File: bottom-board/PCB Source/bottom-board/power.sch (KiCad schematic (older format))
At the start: 22 parts, among them P3 BARREL_JACK, U1 TS2596, U2 TL750M10CKVURG3, U9 LD1117S50TR_SOT223

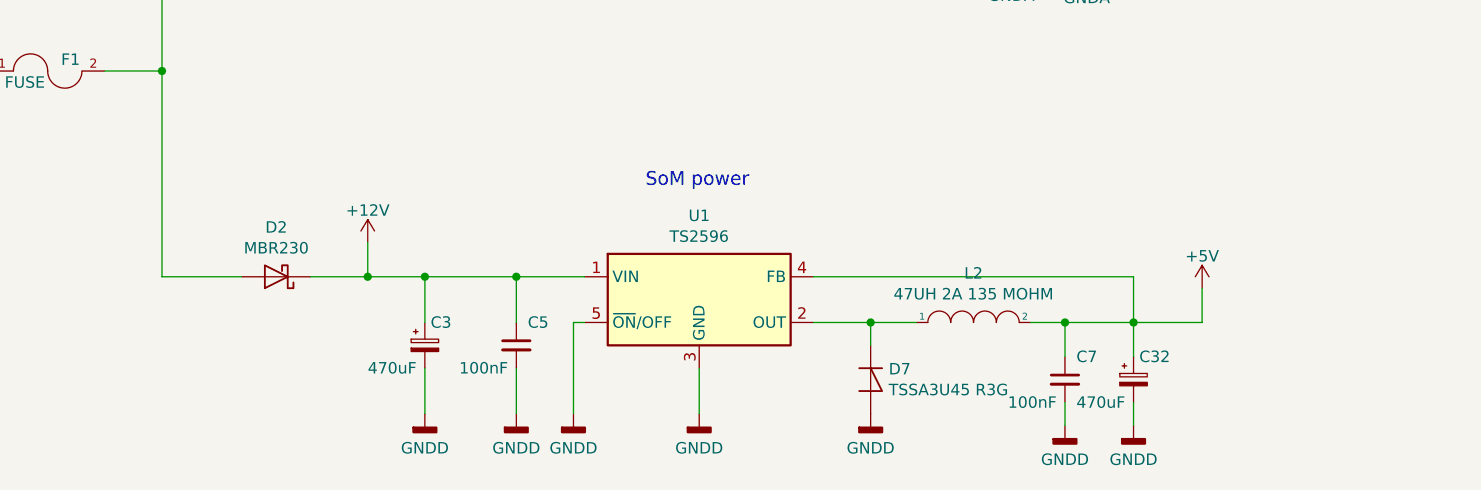
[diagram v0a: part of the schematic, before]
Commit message: increase som filter caps
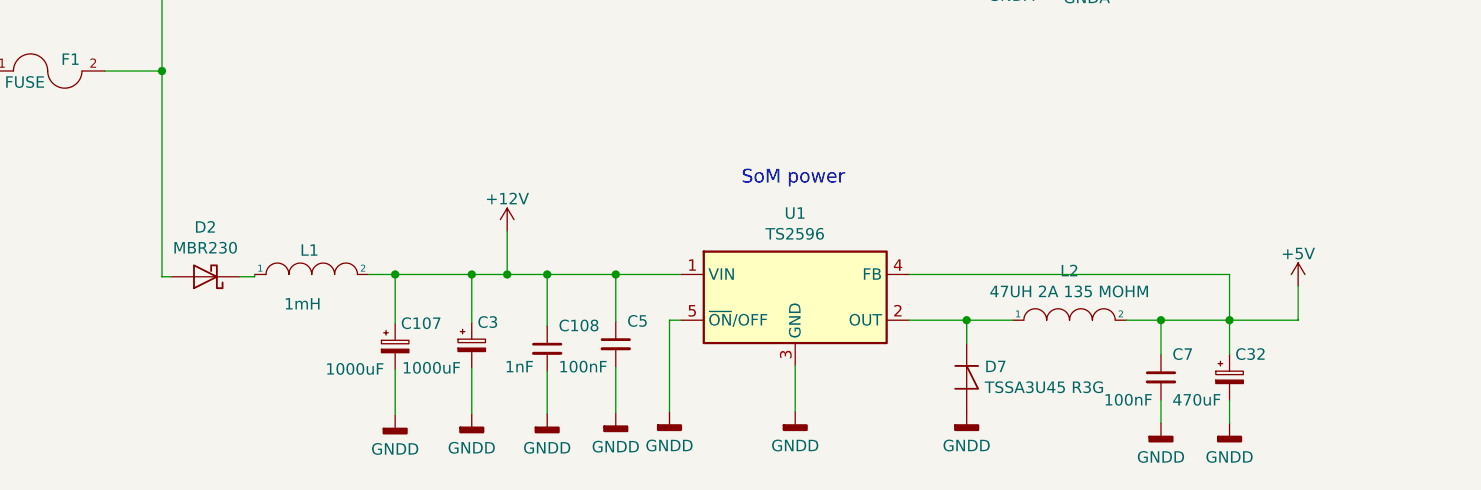
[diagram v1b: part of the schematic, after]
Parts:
- added C107: 1000uF, Uno:CAPAE1300X1400N, symbol bottom-board-rescue:CP_Small
- added C108: 1nF, Capacitor_SMD:C_0603_1608Metric, symbol bottom-board-rescue:C_Small
- added L1: 1mH, Inductor_SMD:L_Bourns_SRR1260, symbol bottom-board-rescue:INDUCTOR-pspice
- C3: value 470uF -> 1000uF; footprint Capacitor_SMD:CP_Elec_8x10.5 -> Uno:CAPAE1300X1400N; MPN UWT1C471MNL1GS -> VE-102M1CTR-1313S
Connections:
- net +12V: now also C107.1, C108.1, L1.2; no longer D2.1 (K)
- net GNDD: now also C107.2, C108.2
- new net: D2.1 (K), L1.1
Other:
- moved on the sheet: C3, C32, C5, C7, D2, D7, L2, U1

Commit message: update fabrication data
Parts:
- U9: MPN (none) -> LD1117S50TR
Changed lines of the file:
@@
 F 2 "Package_TO_SOT_SMD:SOT-223-3_TabPin2" H 6430 3825 50  0001 C CNN
 F 3 "http://www.st.com/st-web-ui/static/active/en/resource/technical/document/datasheet/CD00000544.pdf" H 6530 3375 50  0001 C CNN
+F 4 "LD1117S50TR" H 6430 3625 50  0001 C CNN "MPN"
 	1    6430 3625
 	1    0    0    -1

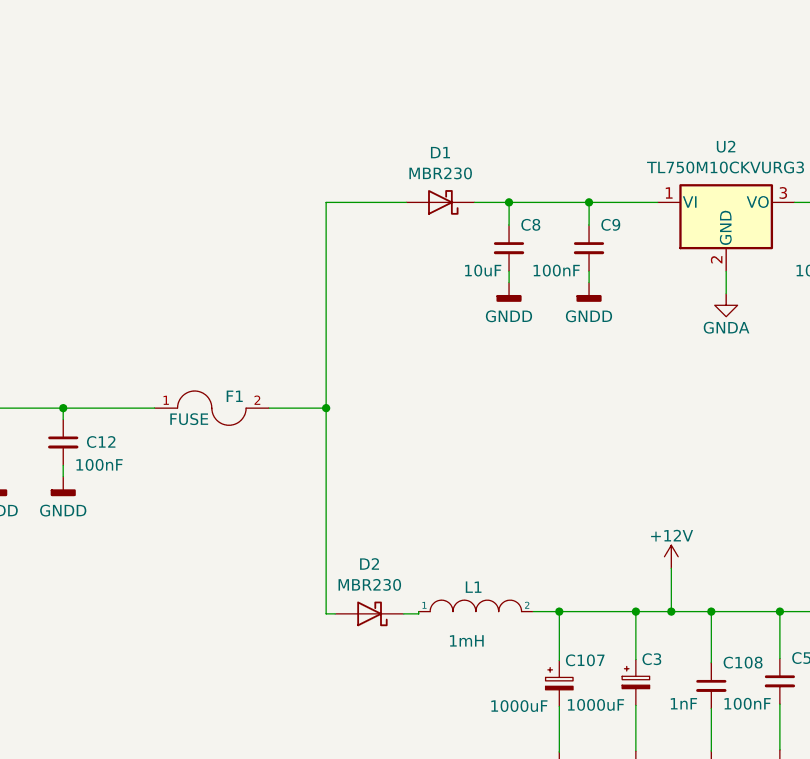
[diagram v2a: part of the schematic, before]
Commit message: change input bias 5->6V, reduce harmonics
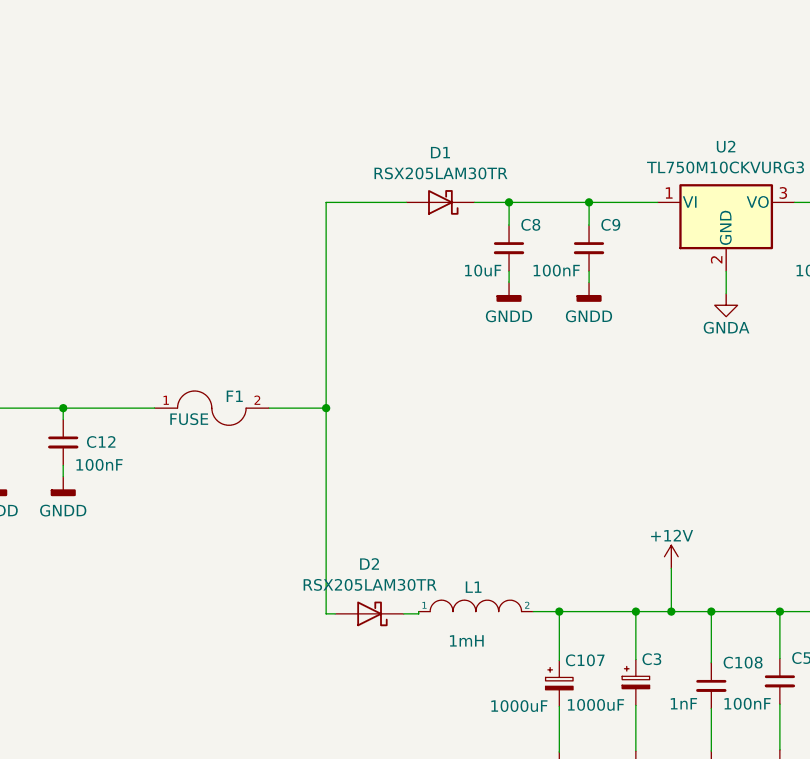
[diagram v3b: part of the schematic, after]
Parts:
- C1: MPN UWX1C101MCL1GB -> 107SML016M
- C107, C3: footprint Uno:CAPAE1300X1400N -> Capacitor_SMD:CP_Elec_10x10.5; MPN VE-102M1CTR-1313S -> UCM1C102MNL1GS
- C32: MPN UWT1C471MNL1GS -> UCW1C471MNL1GS
- D1, D2: value MBR230 -> RSX205LAM30TR; footprint Diode_SMD:D_SOD-123F -> Diode_SMD:D_SOD-128; MPN MBR230LSFT1G -> RSX205LAM30TR
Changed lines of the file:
@@
 P 3590 3625
 F 0 "D1" H 3590 3409 50  0000 C CNN
-F 1 "MBR230" H 3590 3500 50  0000 C CNN
-F 2 "Diode_SMD:D_SOD-123F" H 3590 3625 50  0001 C CNN
+F 1 "RSX205LAM30TR" H 3590 3500 50  0000 C CNN
+F 2 "Diode_SMD:D_SOD-128" H 3590 3625 50  0001 C CNN
 F 3 "~" H 3590 3625 50  0001 C CNN
-F 4 "MBR230LSFT1G" H 3590 3625 50  0001 C CNN "MPN"
+F 4 "RSX205LAM30TR" H 3590 3625 50  0001 C CNN "MPN"
 	1    3590 3625
 	-1   0    0    1
@@
 P 3280 5425
 F 0 "D2" H 3280 5209 50  0000 C CNN
-F 1 "MBR230" H 3280 5300 50  0000 C CNN
-F 2 "Diode_SMD:D_SOD-123F" H 3280 5425 50  0001 C CNN
+F 1 "RSX205LAM30TR" H 3280 5300 50  0000 C CNN
+F 2 "Diode_SMD:D_SOD-128" H 3280 5425 50  0001 C CNN
 F 3 "~" H 3280 5425 50  0001 C CNN
-F 4 "MBR230LSFT1G" H 3280 5425 50  0001 C CNN "MPN"
+F 4 "RSX205LAM30TR" H 3280 5425 50  0001 C CNN "MPN"
 	1    3280 5425
 	-1   0    0    1
@@
 F 0 "C3" H 4470 5825 50  0000 L CNN
 F 1 "1000uF" H 4140 5625 50  0000 L CNN
-F 2 "Uno:CAPAE1300X1400N" H 4483 5575 30  0001 C CNN
+F 2 "Capacitor_SMD:CP_Elec_10x10.5" H 4483 5575 30  0001 C CNN
 F 3 "" H 4445 5725 60  0000 C CNN
-F 4 "VE-102M1CTR-1313S" H 945 2925 50  0001 C CNN "MPN"
+F 4 "UCM1C102MNL1GS" H 945 2925 50  0001 C CNN "MPN"
 	1    4445 5725
 	1    0    0    -1
@@
 F 2 "Capacitor_SMD:CP_Elec_8x10.5" H 7798 5715 30  0001 C CNN
 F 3 "" H 7760 5865 60  0000 C CNN
-F 4 "UWT1C471MNL1GS" H 4260 3065 50  0001 C CNN "MPN"
+F 4 "UCW1C471MNL1GS" H 4260 3065 50  0001 C CNN "MPN"
 	1    7760 5865
 	1    0    0    -1
@@
 F 2 "Capacitor_SMD:CP_Elec_6.3x7.7" H 5778 3675 30  0001 C CNN
 F 3 "" H 5740 3825 60  0000 C CNN
-F 4 "UWX1C101MCL1GB" H 2240 1025 50  0001 C CNN "MPN"
+F 4 "107SML016M" H 2240 1025 50  0001 C CNN "MPN"
 	1    5740 3825
 	1    0    0    -1
@@
 F 0 "C107" H 4135 5830 50  0000 L CNN
 F 1 "1000uF" H 3805 5630 50  0000 L CNN
-F 2 "Uno:CAPAE1300X1400N" H 4148 5580 30  0001 C CNN
+F 2 "Capacitor_SMD:CP_Elec_10x10.5" H 4148 5580 30  0001 C CNN
 F 3 "" H 4110 5730 60  0000 C CNN
-F 4 "VE-102M1CTR-1313S" H 610 2930 50  0001 C CNN "MPN"
+F 4 "UCM1C102MNL1GS" H 610 2930 50  0001 C CNN "MPN"
 	1    4110 5730
 	1    0    0    -1

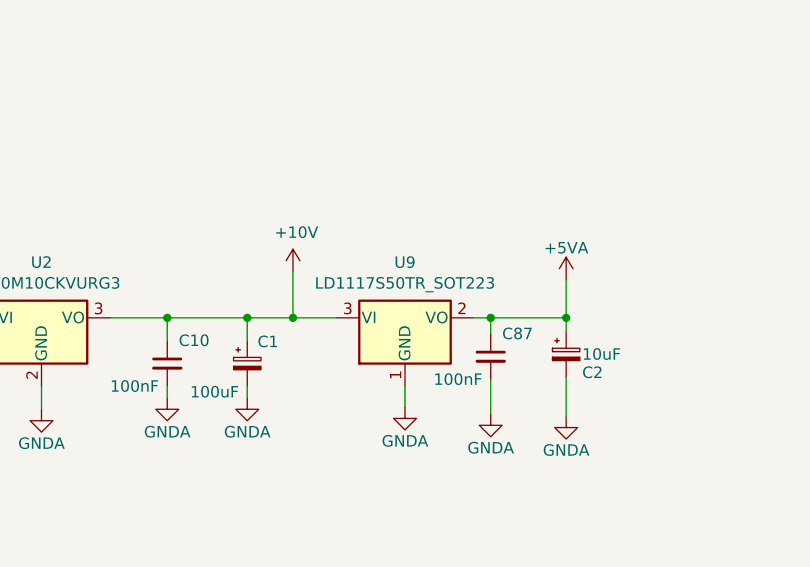
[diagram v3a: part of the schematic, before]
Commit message: change MPN of U10 and U12
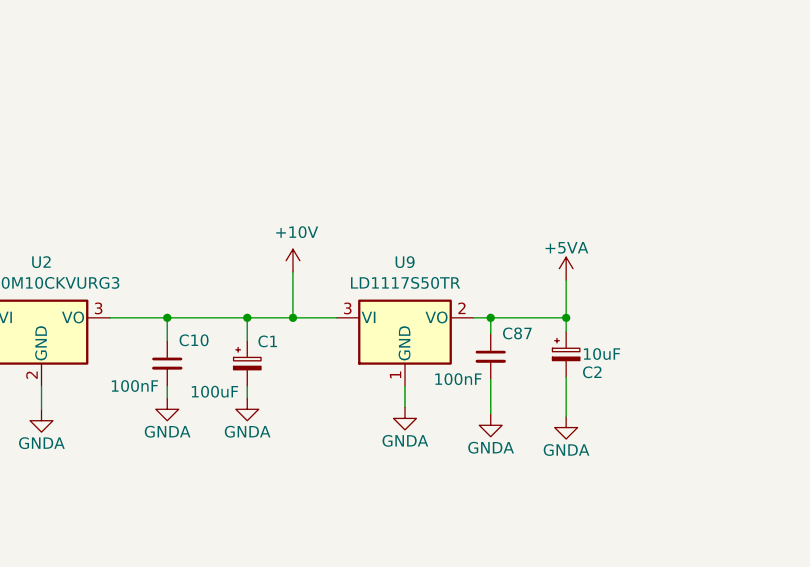
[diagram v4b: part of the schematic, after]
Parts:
- U9: value LD1117S50TR_SOT223 -> LD1117S50TR
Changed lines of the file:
@@
 P 6430 3625
 F 0 "U9" H 6430 3867 50  0000 C CNN
-F 1 "LD1117S50TR_SOT223" H 6430 3776 50  0000 C CNN
+F 1 "LD1117S50TR" H 6430 3776 50  0000 C CNN
 F 2 "Package_TO_SOT_SMD:SOT-223-3_TabPin2" H 6430 3825 50  0001 C CNN
 F 3 "http://www.st.com/st-web-ui/static/active/en/resource/technical/document/datasheet/CD00000544.pdf" H 6530 3375 50  0001 C CNN
